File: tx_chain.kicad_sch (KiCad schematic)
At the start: 7 parts, among them U28 ADRF5703, U29 ADRF5703, U31 MEQ0-20ASM

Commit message: Add Clock sources and monitor output
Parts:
- renumbered R216 to R181, R217 to R182, TP19 to TP14, TP20 to TP15, U28 to U32, U29 to U33, U31 to U34
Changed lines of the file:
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@@
 		(dnp no)
 		(fields_autoplaced yes)
-		(property "Reference" "#PWR0258"
+		(property "Reference" "#PWR0237"
 			(at 101.6 64.77 0)
 			(hide yes)
@@
 			(project "huskypointofload"
 				(path "/eb9c972b-d134-41da-be97-ece3f463f7e0/a878f797-8048-4803-8d22-b5b3217fc43b"
-					(reference "#PWR0258")
+					(reference "#PWR0237")
 					(unit 1)
 				)
@@
 		(dnp no)
 		(fields_autoplaced yes)
-		(property "Reference" "#PWR0259"
+		(property "Reference" "#PWR0236"
 			(at 73.66 77.47 0)
 			(hide yes)
@@
 			(project "huskypointofload"
 				(path "/eb9c972b-d134-41da-be97-ece3f463f7e0/a878f797-8048-4803-8d22-b5b3217fc43b"
-					(reference "#PWR0259")
+					(reference "#PWR0236")
 					(unit 1)
 				)
@@
 		(dnp no)
 		(fields_autoplaced yes)
-		(property "Reference" "#PWR0264"
+		(property "Reference" "#PWR0242"
 			(at 223.52 95.25 0)
 			(hide yes)
@@
 			(project "huskypointofload"
 				(path "/eb9c972b-d134-41da-be97-ece3f463f7e0/a878f797-8048-4803-8d22-b5b3217fc43b"
-					(reference "#PWR0264")
+					(reference "#PWR0242")
 					(unit 1)
 				)
@@
 		(dnp no)
 		(fields_autoplaced yes)
-		(property "Reference" "#PWR0261"
+		(property "Reference" "#PWR0240"
 			(at 173.99 64.77 0)
 			(hide yes)
@@
 			(project "huskypointofload"
 				(path "/eb9c972b-d134-41da-be97-ece3f463f7e0/a878f797-8048-4803-8d22-b5b3217fc43b"
-					(reference "#PWR0261")
+					(reference "#PWR0240")
 					(unit 1)
 				)
@@
 		(in_pos_files yes)
 		(dnp no)
-		(property "Reference" "TP19"
+		(property "Reference" "TP14"
 			(at 27.94 66.04 0)
 			(show_name no)
@@
 			(project "huskypointofload"
 				(path "/eb9c972b-d134-41da-be97-ece3f463f7e0/a878f797-8048-4803-8d22-b5b3217fc43b"
-					(reference "TP19")
+					(reference "TP14")
 					(unit 1)
 				)
@@
 		(in_pos_files yes)
 		(dnp no)
-		(property "Reference" "R216"
+		(property "Reference" "R181"
 			(at 74.93 75.692 90)
 			(show_name no)
@@
 			(project "huskypointofload"
 				(path "/eb9c972b-d134-41da-be97-ece3f463f7e0/a878f797-8048-4803-8d22-b5b3217fc43b"
-					(reference "R216")
+					(reference "R181")
 					(unit 1)
 				)
@@
 		(dnp no)
 		(fields_autoplaced yes)
-		(property "Reference" "U28"
+		(property "Reference" "U32"
 			(at 82.55 64.008 0)
 			(show_name no)
@@
 			(project "huskypointofload"
 				(path "/eb9c972b-d134-41da-be97-ece3f463f7e0/a878f797-8048-4803-8d22-b5b3217fc43b"
-					(reference "U28")
+					(reference "U32")
 					(unit 1)
 				)
@@
 		(dnp no)
 		(fields_autoplaced yes)
-		(property "Reference" "#PWR0263"
+		(property "Reference" "#PWR0241"
 			(at 182.88 123.19 0)
 			(hide yes)
@@
 			(project "huskypointofload"
 				(path "/eb9c972b-d134-41da-be97-ece3f463f7e0/a878f797-8048-4803-8d22-b5b3217fc43b"
-					(reference "#PWR0263")
+					(reference "#PWR0241")
 					(unit 1)
 				)
@@
 		(dnp no)
 		(fields_autoplaced yes)
-		(property "Reference" "#PWR0262"
+		(property "Reference" "#PWR0238"
 			(at 110.49 123.19 0)
 			(hide yes)
@@
 			(project "huskypointofload"
 				(path "/eb9c972b-d134-41da-be97-ece3f463f7e0/a878f797-8048-4803-8d22-b5b3217fc43b"
-					(reference "#PWR0262")
+					(reference "#PWR0238")
 					(unit 1)
 				)
@@
 		(dnp no)
 		(fields_autoplaced yes)
-		(property "Reference" "#PWR0257"
+		(property "Reference" "#PWR0235"
 			(at 38.1 96.52 0)
 			(hide yes)
@@
 			(project "huskypointofload"
 				(path "/eb9c972b-d134-41da-be97-ece3f463f7e0/a878f797-8048-4803-8d22-b5b3217fc43b"
-					(reference "#PWR0257")
+					(reference "#PWR0235")
 					(unit 1)
 				)
@@
 		(dnp no)
 		(fields_autoplaced yes)
-		(property "Reference" "U31"
+		(property "Reference" "U34"
 			(at 223.52 58.42 0)
 			(show_name no)
@@
 			(project "huskypointofload"
 				(path "/eb9c972b-d134-41da-be97-ece3f463f7e0/a878f797-8048-4803-8d22-b5b3217fc43b"
-					(reference "U31")
+					(reference "U34")
 					(unit 1)
 				)
@@
 		(in_pos_files yes)
 		(dnp no)
-		(property "Reference" "R217"
+		(property "Reference" "R182"
 			(at 147.32 75.692 90)
 			(show_name no)
@@
 			(project "huskypointofload"
 				(path "/eb9c972b-d134-41da-be97-ece3f463f7e0/a878f797-8048-4803-8d22-b5b3217fc43b"
-					(reference "R217")
+					(reference "R182")
 					(unit 1)
 				)
@@
 		(dnp no)
 		(fields_autoplaced yes)
-		(property "Reference" "U29"
+		(property "Reference" "U33"
 			(at 154.94 64.008 0)
 			(show_name no)
@@
 			(project "huskypointofload"
 				(path "/eb9c972b-d134-41da-be97-ece3f463f7e0/a878f797-8048-4803-8d22-b5b3217fc43b"
-					(reference "U29")
+					(reference "U33")
 					(unit 1)
 				)
@@
 		(dnp no)
 		(fields_autoplaced yes)
-		(property "Reference" "#PWR0260"
+		(property "Reference" "#PWR0239"
 			(at 146.05 77.47 0)
 			(hide yes)
@@
 			(project "huskypointofload"
 				(path "/eb9c972b-d134-41da-be97-ece3f463f7e0/a878f797-8048-4803-8d22-b5b3217fc43b"
-					(reference "#PWR0260")
+					(reference "#PWR0239")
 					(unit 1)
 				)
@@
 		(in_pos_files yes)
 		(dnp no)
-		(property "Reference" "TP20"
+		(property "Reference" "TP15"
 			(at 48.26 66.04 0)
 			(show_name no)
@@
 			(project "huskypointofload"
 				(path "/eb9c972b-d134-41da-be97-ece3f463f7e0/a878f797-8048-4803-8d22-b5b3217fc43b"
-					(reference "TP20")
-					(unit 1)
-				)
+					(reference "TP15")
+					(unit 1)
+				)

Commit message: Round 1 review comments
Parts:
- added C? (x4): 100n, Capacitor_SMD:C_0402_1005Metric, symbol Device:C_Small
- renumbered R181 to R244, R182 to R245, TP14 to TP15, TP15 to TP16, U32 to U35, U33 to U36, U34 to U37
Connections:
- net +3.3V: now also C?.1, C?.1, C?.1, C?.1
- net GND: now also C?.2, C?.2, C?.2, C?.2

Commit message: Round 2 Review, power tree cleanup
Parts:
- added C? (x2): 1u, symbol Device:C_Small
- added U?: TLV73333PDBV, Package_TO_SOT_SMD:SOT-23-5, symbol Regulator_Linear:TLV73333PDBV
- gave numbers to parts that had none: 4
- renumbered R244 to R257, R245 to R258, U35 to U36, U36 to U37, U37 to U38
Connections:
- net +3.3V: no longer C239.1, C240.1, C241.1, C242.1, U36.18 (VDD), U37.18 (VDD)
- net GND: now also C?.2, C?.2, U?.2 (GND)
- new net +4V: C?.1, U?.1 (IN), U?.3 (EN)
- new net VCC_TX_DIG: C239.1, C240.1, C241.1, C242.1, C?.1, U36.18 (VDD), U37.18 (VDD), U?.5 (OUT)

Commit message: Darrel Suggestions
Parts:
- added C246: 1n, Capacitor_SMD:C_0201_0603Metric, symbol Device:C_Small
- R257, R258: footprint Package_BGA:TFBGA-100_8x8mm_Layout10x10_P0.8mm -> (none)
- U37: renamed from U36; footprint Package_SO:MSOP-10_3x3mm_P0.5mm -> (none)
- U38: renamed from U37; footprint Package_SO:MSOP-10_3x3mm_P0.5mm -> (none)
- U39: renamed from U38; footprint Package_SO:MSOP-10_3x3mm_P0.5mm -> (none)
- gave numbers to parts that had none: 3
- renumbered C239 to C242, C240 to C243, C241 to C244, C242 to C245, TP15 to TP12, TP16 to TP13
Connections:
- net RFOUT: now also C246.1; no longer U39.9 (RFOUT)
- new net: C246.2, U39.9 (RFOUT)

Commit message: Passive footprint pass
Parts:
- C240, C241: footprint (none) -> Capacitor_SMD:C_0402_1005Metric
- R257, R258: footprint (none) -> Resistor_SMD:R_0402_1005Metric
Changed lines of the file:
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@@
 			)
 		)
-		(property "Footprint" ""
+		(property "Footprint" "Resistor_SMD:R_0402_1005Metric"
 			(at 74.93 77.47 0)
 			(hide yes)
@@
 			)
 		)
-		(property "Footprint" ""
+		(property "Footprint" "Capacitor_SMD:C_0402_1005Metric"
 			(at 38.1 34.29 0)
 			(hide yes)
@@
 			)
 		)
-		(property "Footprint" ""
+		(property "Footprint" "Resistor_SMD:R_0402_1005Metric"
 			(at 147.32 77.47 0)
 			(hide yes)
@@
 			)
 		)
-		(property "Footprint" ""
+		(property "Footprint" "Capacitor_SMD:C_0402_1005Metric"
 			(at 63.5 34.29 0)
 			(hide yes)

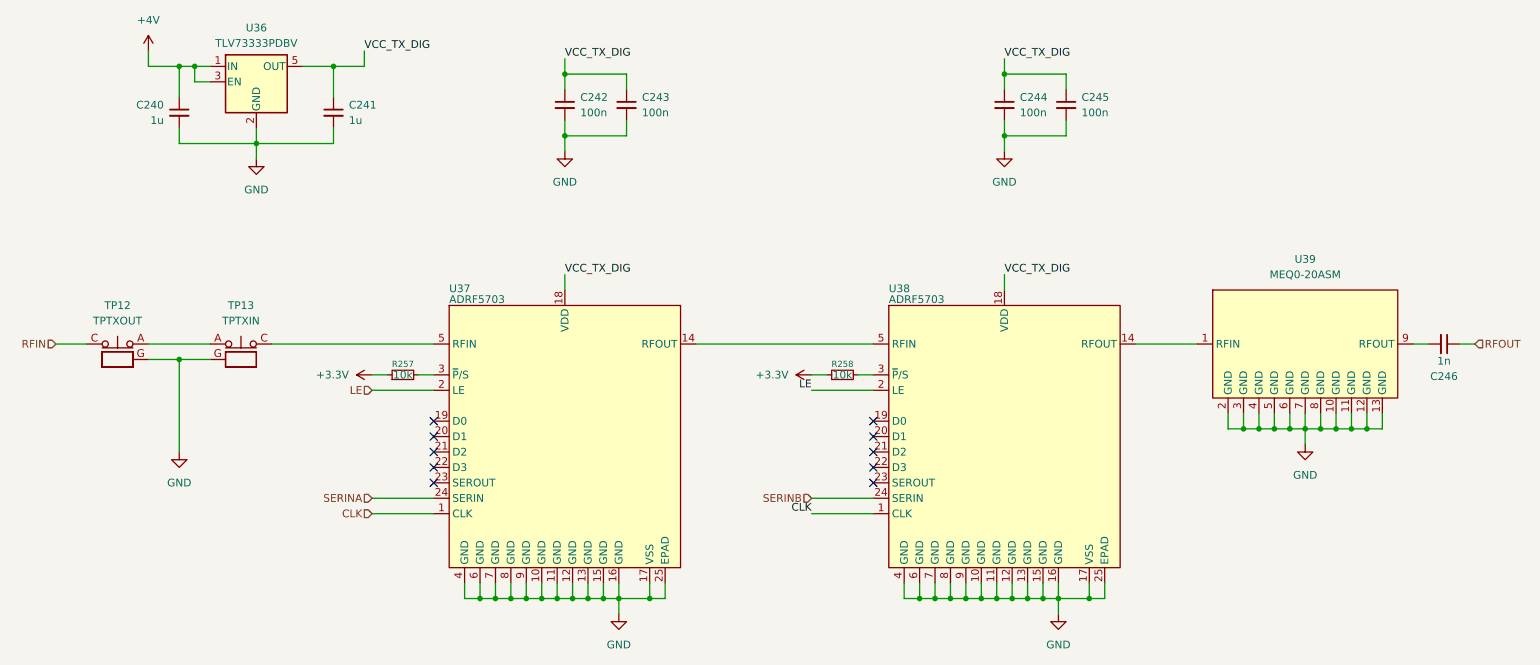
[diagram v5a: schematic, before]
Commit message: add NC and fix ERC
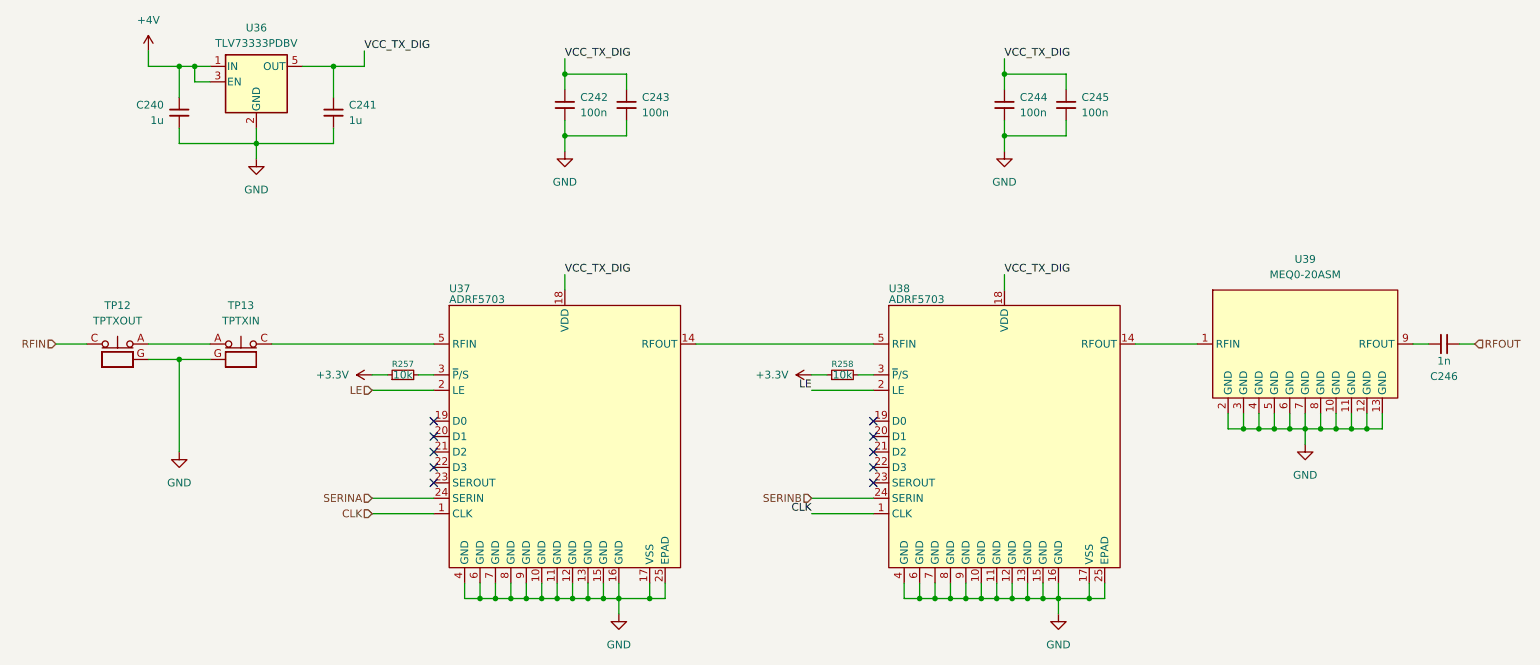
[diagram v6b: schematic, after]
